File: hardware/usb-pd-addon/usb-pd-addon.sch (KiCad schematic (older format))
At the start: 75 parts, among them J1 Conn_02x10_Odd_Even, J11 Conn_02x02, J2 Conn_02x10_Odd_Even, J3 USB_TYPE_C, J4 USB_TYPE_C, J6 TPAS, J7 TPBS, J8 Conn_02x03_Odd_Even, J9 Conn_02x02, U1 FUSB302B, U10 NC7SB3157P6X, U11 NC7SB3157P6X, U2 AP2171W, U3 SN74AVC1T45DCKR, U4 SN74AVC1T45DCKR, U5 SN74AVC1T45DCKR, U6 SN74AVC1T45DBVR, U7 AP2127K-ADJ, U8 NC7SB3157P6X, U9 NC7SB3157P6X

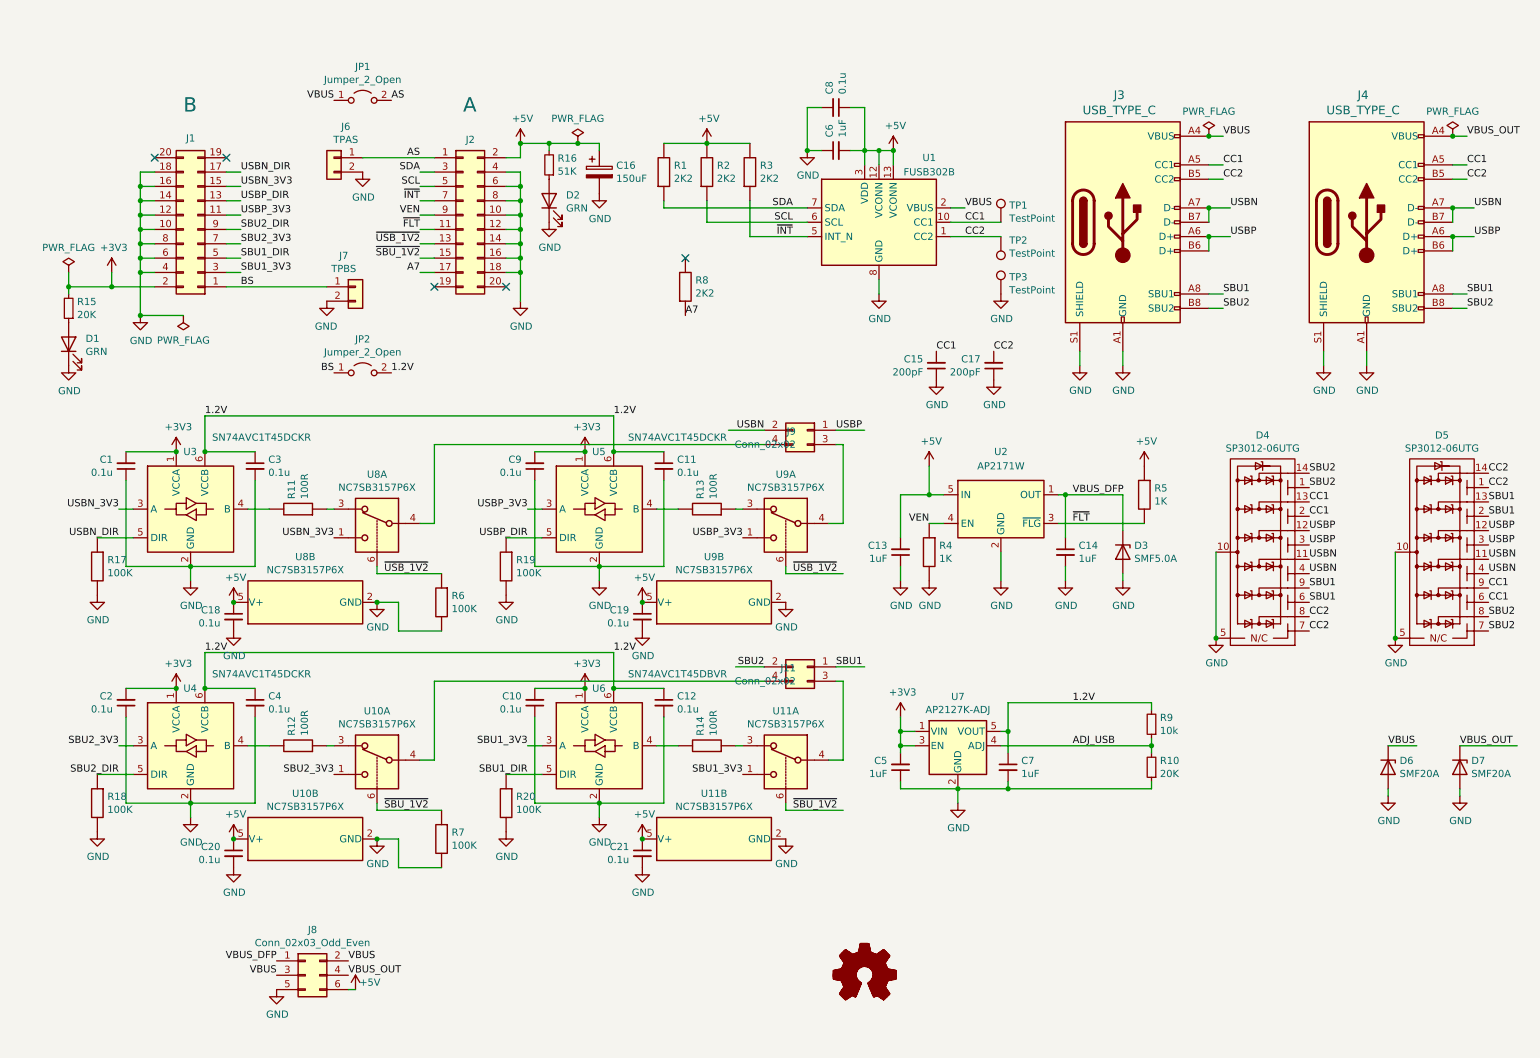
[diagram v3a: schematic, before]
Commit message: v0.8b: Lots of silk improvements on front side. Relayout of center column of wires. Extended USB-C connectors past board edge.
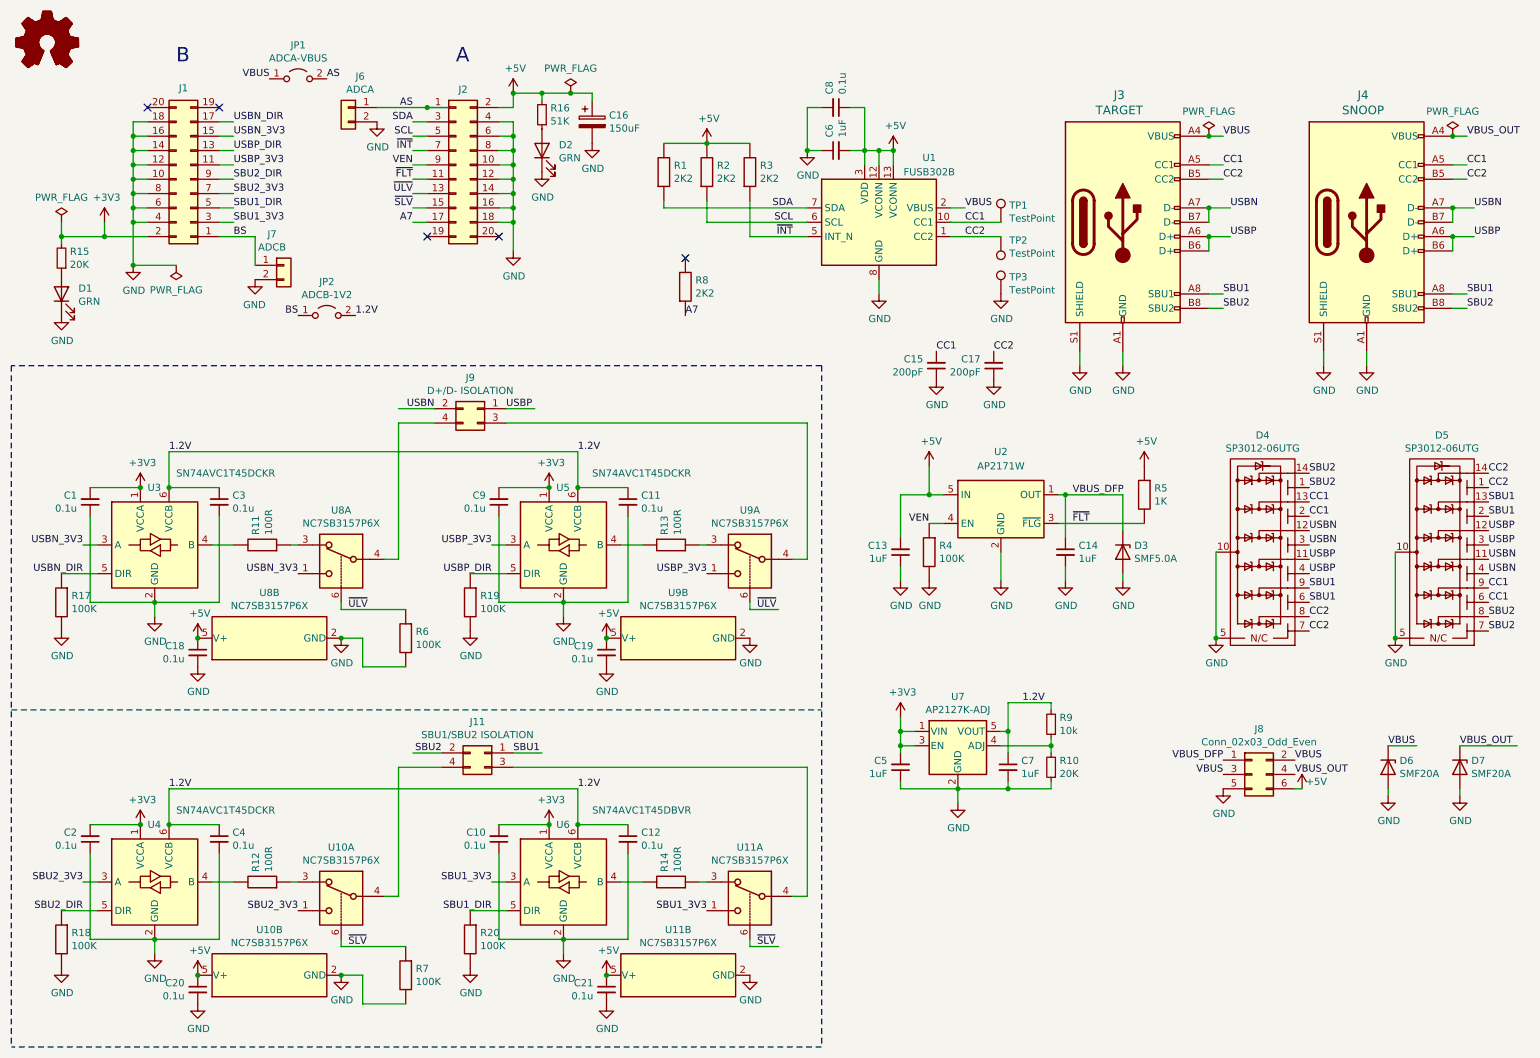
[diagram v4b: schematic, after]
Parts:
- J11: value Conn_02x02 -> SBU1/SBU2 ISOLATION
- J3: value USB_TYPE_C -> TARGET
- J4: value USB_TYPE_C -> SNOOP
- J6: value TPAS -> ADCA
- J7: value TPBS -> ADCB
- J9: value Conn_02x02 -> D+/D- ISOLATION
- JP1: value Jumper_2_Open -> ADCA-VBUS
- JP2: value Jumper_2_Open -> ADCB-1V2
- R4: value 1K -> 100K; LCSC C21190 -> C25803
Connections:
- net labels added: ~SLV, ~ULV
- net labels removed: ADJ_USB, ~SBU_1V2, ~USB_1V2
- wire segments 229 -> 231
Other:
- moved on the sheet: C1, C10, C11, C12, C16, C18, C19, C2, C20, C21, C3, C4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

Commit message: Ordered annotations and rotated components.
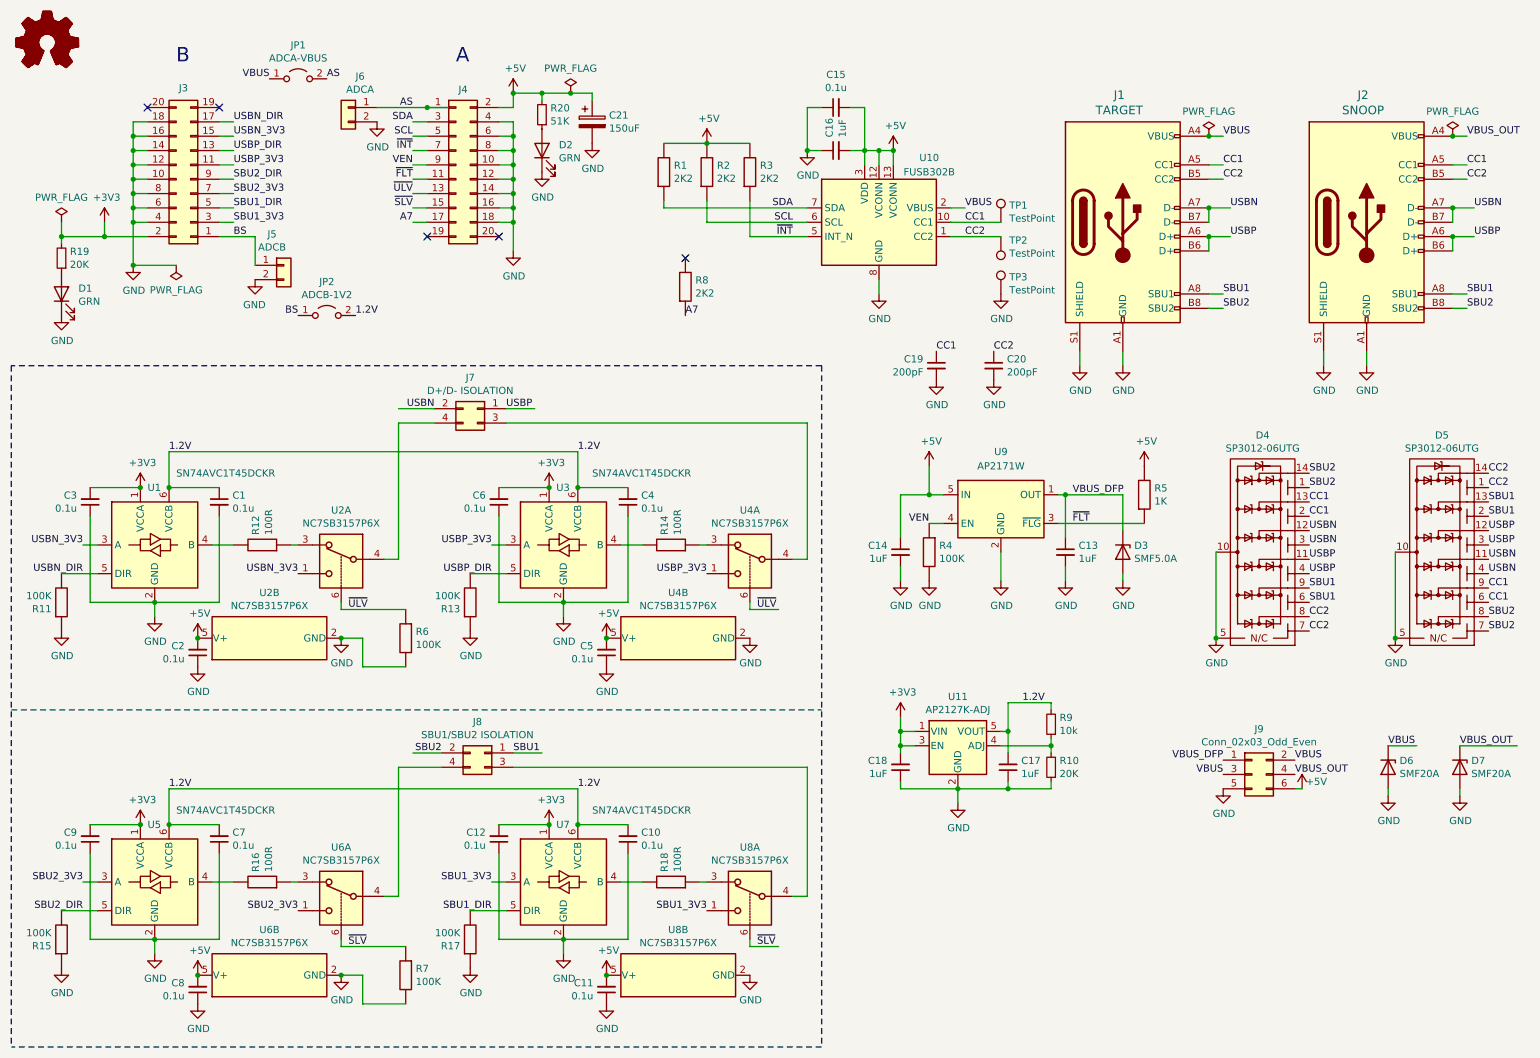
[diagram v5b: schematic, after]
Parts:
- R12: renamed from R11; LCSC (none) -> C22775
- R14: renamed from R13; LCSC (none) -> C22775
- R16: renamed from R12; LCSC (none) -> C22775
- R18: renamed from R14; LCSC (none) -> C22775
- U2: renamed from U8; LCSC (none) -> C87403
- U4: renamed from U9; LCSC (none) -> C87403
- U6: renamed from U10; LCSC (none) -> C87403
- U7: renamed from U6; value SN74AVC1T45DBVR -> SN74AVC1T45DCKR
- U8: renamed from U11; LCSC (none) -> C87403
- renumbered C3 to C1, C12 to C10, C21 to C11, C10 to C12, C14 to C13, C13 to C14, C8 to C15, C6 to C16, C7 to C17, C5 to C18, C15 to C19, C18 to C2, C17 to C20, C16 to C21, C1 to C3, C11 to C4, C19 to C5, C9 to C6, C4 to C7, C20 to C8, C2 to C9, J3 to J1, J4 to J2, J1 to J3, J2 to J4, J7 to J5, J9 to J7, J11 to J8, J8 to J9, R17 to R11, R19 to R13, R18 to R15, R20 to R17, R15 to R19, R16 to R20, U3 to U1, U1 to U10, U7 to U11, U5 to U3, U4 to U5, U2 to U9

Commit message: v0.8c: Added 1.2V test point and more front silk improvements.
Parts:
- added TP4: TestPoint, TestPoint:TestPoint_THTPad_1.0x1.0mm_Drill0.5mm, symbol Connector:TestPoint
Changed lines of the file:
@@
 Title "USB-PD on Glasgow"
 Date ""
-Rev "V0.8b"
+Rev "V0.8c"
 Comp "License: CC-BY-SA 4.0"
 Comment1 "(C) 2020-2021 Piotr Esden-Tempski <piotr@esden.net>"
@@
 Connection ~ 1800 7250
 Connection ~ 4650 7250
+$Comp
+L Connector:TestPoint TP4
+U 1 1 604A12CC
+P 7750 5350
+F 0 "TP4" H 7808 5468 50  0000 L CNN
+F 1 "TestPoint" H 7808 5377 50  0000 L CNN
+F 2 "TestPoint:TestPoint_THTPad_1.0x1.0mm_Drill0.5mm" H 7950 5350 50  0001 C CNN
+F 3 "~" H 7950 5350 50  0001 C CNN
+	1    7750 5350
+	1    0    0    -1
+$EndComp
+Connection ~ 7750 5350
 $EndSCHEMATC
